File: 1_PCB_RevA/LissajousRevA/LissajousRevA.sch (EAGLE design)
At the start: 0 parts

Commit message: first relax osc and lpf
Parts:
- added C1, C2, C3, C4, C5: (no value), passives:CAP0603-CAP
- added R1, R10, R2, R3, R4, R5, R6, R7, R8, R9: (no value), passives:RESISTOR0603-RES
- added TM1: 200K, adafruit:TRIMPOTTC33X
- added TP1, TP2, TP3: TEST-POINT3, passives:TEST-POINT3
- added U1: LM348D, LM348D:LM348D
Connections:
- new net 0V: C1.1, C2.1, C4.1, R1.1
- new net N$1: C1.2, R3.1, U1D.IN-
- new net N$11: C4.2, R8.1, U1B.IN+
- new net N$12: C5.1, R5.1, R8.2
- new net N$13: C5.2, TP3.1, U1B.IN-, U1B.OUT
- new net N$14: R10.1, R5.2
- new net N$2: R1.2, R2.1, U1D.IN+
- new net N$3: R6.2, R9.1
- new net N$4: R3.2, R4.2, TM1.E, TM1.S
- new net N$5: C2.2, R7.1, U1A.IN+
- new net N$6: C3.1, R6.1, R7.2
- new net N$7: R2.2, R4.1, R9.2, TM1.A, TP1.1, U1D.OUT
- new net N$8: C3.2, R10.2, TP2.1, U1A.IN-, U1A.OUT
- new net V+: U1A.+
- new net V-: U1A.-

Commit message: added second gen
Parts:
- added C10, C6, C7, C8, C9: (no value), passives:CAP0603-CAP
- added R11, R12, R13, R14, R15, R16, R17, R18, R19, R20: (no value), passives:RESISTOR0603-RES
- added TM2: 200K, adafruit:TRIMPOTTC33X
- added TP4, TP5, TP6: TEST-POINT3, passives:TEST-POINT3
- added U2: LM348D, LM348D:LM348D
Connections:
- net N$13 renamed SINEGEN1
- new net N$10: C6.2, R13.1, U2D.IN-
- new net N$15: R12.2, R14.1, R19.2, TM2.A, TP4.1, U2D.OUT
- new net N$16: C7.2, R16.1, U2A.IN+
- new net N$17: C8.1, R15.1, R16.2
- new net N$18: C9.2, R18.1, U2B.IN+
- new net N$19: C10.1, R17.1, R18.2
- new net N$21: C8.2, R20.2, TP5.1, U2A.IN-, U2A.OUT
- new net N$22: R15.2, R19.1
- new net N$23: R17.2, R20.1
- new net N$24: R13.2, R14.2, TM2.E, TM2.S
- new net N$9: R11.2, R12.1, U2D.IN+
- new net SINEGEN2: C10.2, TP6.1, U2B.IN-, U2B.OUT
- net 0V: now also C6.1, C7.1, C9.1, R11.1
- net V+: now also U2A.+
- net V-: now also U2A.-
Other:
- note added: "Sine generation 1"
- note added: "Sine generation 2"
- moved on the sheet: C1, C2, C3, C4, C5, R1, R10, R2, R3, R4, R5, R6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

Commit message: schmatics have everything down
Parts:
- removed C1, C10, C2, C3, C4, C5, C6, C7, C8, C9: (no value), passives:CAP0603-CAP
- removed R1, R10, R11, R12, R13, R14, R15, R16, R17, R18, R19, R2, R20, R3, R4, R5, R6, R7, R8, R9: (no value), passives:RESISTOR0603-RES
- removed TM1, TM2: 200K, adafruit:TRIMPOTTC33X
- removed TP5, TP6: TEST-POINT3, passives:TEST-POINT3
- removed U1, U2: LM348D, LM348D:LM348D
- added C101, C102, C103, C104, C105, C201, C202, C203, C204, C205: 4.7nF, passives:CAP0603-CAP
- added C301, C302, C303, C304, C305, C306, C402: 100nF, passives:CAP0603-CAP
- added C401: 100pF, passives:CAP0603-CAP
- added C501, C502, C503, C504, C505, C506: 10nF, passives:CAP0603-CAP
- added D401: 1N4148, adafruit:DIODESMA
- added Q401, Q501, Q502, Q503: (no value), adafruit:MOSFET-NREFLOW
- added R101, R201, R403, R405, R407: DNF, passives:RESISTOR0603-RES
- added R102, R202, R408, R503: 200K, adafruit:TRIMPOTTC33X
- added R103: 5K, passives:RESISTOR0603-RES
- added R104, R105, R107, R108, R110, R111, R204, R205, R207, R208, R210, R211, R501, R502, R504, R505, R506, R507, R508, R509, R510: 33K, passives:RESISTOR0603-RES
- added R106, R109, R206, R209, R402: 0R, passives:RESISTOR0603-RES
- added R203, R406: 5K6, passives:RESISTOR0603-RES
- added R401: 1M, passives:RESISTOR0603-RES
- added R404: 100K, passives:RESISTOR0603-RES
- added TP101, TP102, TP103, TP201, TP202, TP203, TP401, TP402: TEST-POINT3, passives:TEST-POINT3
- added TP301, TP302, TP303: TEST-POINTTP_15TH_THRU, passives:TEST-POINTTP_15TH_THRU
- added U101, U201, U401: LM348D, LM348D:LM348D
- TP3, TP4: value TEST-POINT3 -> TEST-POINTTP_15TH_THRU; device passives:TEST-POINT3 -> passives:TEST-POINTTP_15TH_THRU
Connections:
- new net N$13: R401.2, R402.1, U101C.IN-
- new net N$20: C501.1, Q501.D, U401A.IN+
- new net N$25: C402.2, R406.2, R407.2, U401C.IN-
- new net N$26: R501.2, R502.1, U401A.IN-
- new net N$27: R404.2, U401B.IN-
- new net N$28: D401.A, U401B.OUT
- new net N$29: C502.1, C503.2, R504.2, R505.1, TP1.1
- new net N$30: C401.2, D401.C, R404.1, R405.1, R406.1, TP401.1
- new net N$31: Q401.D, R402.2, R403.1
- new net N$32: C402.1, Q401.G, R407.1, TP402.1, U401C.OUT
- new net N$33: C502.2, R502.2, U401A.OUT
- new net N$34: R408.S, U401C.IN+
- new net N$35: C506.2
- new net N$36: C503.1, Q502.D, U401D.IN+
- new net N$37: R505.2, R506.1, U401D.IN-
- new net N$38: Q501.G, Q502.G, Q503.G, R503.S
- new net N$39: R506.2, U401D.OUT
- new net N$40: R508.2, R509.1, U201C.IN-
- new net N$41: C504.2
- new net N$42: C504.1, C505.2, R507.2, R508.1, TP2.1
- new net N$45: C505.1, Q503.D, U201C.IN+
- new net N$46: R509.2, U201C.OUT
- new net VIEW1: R401.1, TP4.1, U101C.OUT, U401B.IN+
- new net VIEW2: C506.1, R510.2, TP3.1
- net 0V: now also C101.1, C103.1, C105.1, C201.1, C203.1, C205.1, C301.1, C302.1, C303.1, C304.2, C305.2, C306.2, C401.1, Q401.S, Q501.S, Q502.S, Q503.S, R105.1, R205.1, R403.2, R405.2, R408.E, R503.A, R504.1, R507.1, R510.1, TP302.1; no longer C1.1, C2.1, C4.1, C6.1, C7.1, C9.1, R1.1, R11.1
- net N$1: now also C101.2, R103.1, U101D.IN-; no longer C1.2, R3.1, U1D.IN-
- net N$10: now also C201.2, R203.1, U201D.IN-; no longer C6.2, R13.1, U2D.IN-
- net N$11: now also C105.2, R111.1, U101B.IN+; no longer C4.2, R8.1, U1B.IN+
- net N$12: now also C104.1, R110.1, R111.2; no longer C5.1, R5.1, R8.2
- net N$14: now also R109.1, R110.2; no longer R10.1, R5.2
- net N$15: now also R201.1, R202.A, R204.2, R206.2, TP201.1, U201D.OUT; no longer R12.2, R14.1, R19.2, TM2.A, TP4.1, U2D.OUT
- net N$16: now also C203.2, R208.1, U201A.IN+; no longer C7.2, R16.1, U2A.IN+
- net N$17: now also C202.1, R207.1, R208.2; no longer C8.1, R15.1, R16.2
- net N$18: now also C205.2, R211.1, U201B.IN+; no longer C9.2, R18.1, U2B.IN+
- net N$19: now also C204.1, R210.1, R211.2; no longer C10.1, R17.1, R18.2
- net N$2: now also R104.1, R105.2, U101D.IN+; no longer R1.2, R2.1, U1D.IN+
- net N$21: now also C202.2, R209.2, TP202.1, U201A.IN-, U201A.OUT; no longer C8.2, R20.2, TP5.1, U2A.IN-, U2A.OUT
- net N$22: now also R206.1, R207.2; no longer R15.2, R19.1
- net N$23: now also R209.1, R210.2; no longer R17.2, R20.1
- net N$24: now also R201.2, R202.E, R202.S, R203.2; no longer R13.2, R14.2, TM2.E, TM2.S
- net N$3: now also R106.1, R107.2; no longer R6.2, R9.1
- net N$4: now also R101.2, R102.E, R102.S, R103.2; no longer R3.2, R4.2, TM1.E, TM1.S
- net N$5: now also C103.2, R108.1, U101A.IN+; no longer C2.2, R7.1, U1A.IN+
- net N$6: now also C102.1, R107.1, R108.2; no longer C3.1, R6.1, R7.2
- net N$7: now also R101.1, R102.A, R104.2, R106.2, TP101.1, U101D.OUT; no longer R2.2, R4.1, R9.2, TM1.A, TP1.1, U1D.OUT
- net N$8: now also C102.2, R109.2, TP102.1, U101A.IN-, U101A.OUT; no longer C3.2, R10.2, TP2.1, U1A.IN-, U1A.OUT
- net N$9: now also R204.1, R205.2, U201D.IN+; no longer R11.2, R12.1, U2D.IN+
- net SINEGEN1: now also C104.2, TP103.1, U101B.IN-, U101B.OUT, U101C.IN+; no longer C5.2, TP3.1, U1B.IN-, U1B.OUT
- net SINEGEN2: now also C204.2, C501.2, R501.1, TP203.1, U201B.IN-, U201B.OUT; no longer C10.2, TP6.1, U2B.IN-, U2B.OUT
- net V+: now also C301.2, C302.2, C303.2, R408.A, R503.E, TP301.1, U101A.+, U201A.+, U401A.+; no longer U1A.+, U2A.+
- net V-: now also C304.1, C305.1, C306.1, TP303.1, U101A.-, U201A.-, U401A.-; no longer U1A.-, U2A.-
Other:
- note added: "Automatic gain control"
- note added: "Phase shift"
- note added: "Support"
- moved on the sheet: TP1, TP2, TP3, TP4

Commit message: schematic capture done
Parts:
- renumbered TP1 to TP501, TP2 to TP502, TP3 to TP305, TP4 to TP304
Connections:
- net 0V: now also TP303.1; no longer TP302.1
- net V-: now also TP302.1; no longer TP303.1
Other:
- moved on the sheet: TP302, TP303
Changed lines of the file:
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@@
 <part name="TP203" library="passives" deviceset="TEST-POINT" device="3"/>
 <part name="TP301" library="passives" deviceset="TEST-POINT" device="TP_15TH_THRU"/>
-<part name="TP302" library="passives" deviceset="TEST-POINT" device="TP_15TH_THRU"/>
+<part name="TP303" library="passives" deviceset="TEST-POINT" device="TP_15TH_THRU"/>
 <part name="C301" library="passives" deviceset="CAP" device="0603-CAP" value="100nF"/>
 <part name="C302" library="passives" deviceset="CAP" device="0603-CAP" value="100nF"/>
@@
 <part name="V12" library="supply" deviceset="V+" device=""/>
 <part name="V13" library="supply" deviceset="V-" device=""/>
-<part name="TP303" library="passives" deviceset="TEST-POINT" device="TP_15TH_THRU"/>
+<part name="TP302" library="passives" deviceset="TEST-POINT" device="TP_15TH_THRU"/>
 <part name="C303" library="passives" deviceset="CAP" device="0603-CAP" value="100nF"/>
 <part name="C304" library="passives" deviceset="CAP" device="0603-CAP" value="100nF"/>
@@
 <part name="R510" library="passives" deviceset="RESISTOR" device="0603-RES" value="33K"/>
 <part name="V31" library="supply" deviceset="0V" device=""/>
-<part name="TP1" library="passives" deviceset="TEST-POINT" device="3"/>
-<part name="TP2" library="passives" deviceset="TEST-POINT" device="3"/>
-<part name="TP3" library="passives" deviceset="TEST-POINT" device="TP_15TH_THRU"/>
-<part name="TP4" library="passives" deviceset="TEST-POINT" device="TP_15TH_THRU"/>
+<part name="TP501" library="passives" deviceset="TEST-POINT" device="3"/>
+<part name="TP502" library="passives" deviceset="TEST-POINT" device="3"/>
+<part name="TP305" library="passives" deviceset="TEST-POINT" device="TP_15TH_THRU"/>
+<part name="TP304" library="passives" deviceset="TEST-POINT" device="TP_15TH_THRU"/>
 </parts>
 <sheets>
@@
 <instance part="TP203" gate="G$1" x="256.54" y="152.4"/>
 <instance part="TP301" gate="G$1" x="317.5" y="243.84"/>
-<instance part="TP302" gate="G$1" x="340.36" y="226.06"/>
+<instance part="TP303" gate="G$1" x="340.36" y="226.06"/>
 <instance part="C301" gate="G$1" x="302.26" y="205.74" rot="R180"/>
 <instance part="C302" gate="G$1" x="314.96" y="205.74" rot="R180"/>
@@
 <instance part="V12" gate="1" x="297.18" y="243.84" rot="R90"/>
 <instance part="V13" gate="1" x="297.18" y="236.22" rot="R270"/>
-<instance part="TP303" gate="G$1" x="317.5" y="236.22"/>
+<instance part="TP302" gate="G$1" x="317.5" y="236.22"/>
 <instance part="C303" gate="G$1" x="327.66" y="205.74" rot="R180"/>
 <instance part="C304" gate="G$1" x="340.36" y="205.74" rot="R180"/>
@@
 <instance part="R510" gate="G$1" x="350.52" y="109.22" rot="R90"/>
 <instance part="V31" gate="1" x="350.52" y="99.06"/>
-<instance part="TP1" gate="G$1" x="266.7" y="78.74" rot="R180"/>
-<instance part="TP2" gate="G$1" x="347.98" y="86.36"/>
-<instance part="TP3" gate="G$1" x="325.12" y="175.26" rot="R180"/>
-<instance part="TP4" gate="G$1" x="332.74" y="182.88"/>
+<instance part="TP501" gate="G$1" x="266.7" y="78.74" rot="R180"/>
+<instance part="TP502" gate="G$1" x="347.98" y="86.36"/>
+<instance part="TP305" gate="G$1" x="325.12" y="175.26" rot="R180"/>
+<instance part="TP304" gate="G$1" x="332.74" y="182.88"/>
 </instances>
 <busses>
@@
 </segment>
 <segment>
-<pinref part="TP303" gate="G$1" pin="1"/>
+<pinref part="TP302" gate="G$1" pin="1"/>
 <wire x1="317.5" y1="236.22" x2="299.72" y2="236.22" width="0.1524" layer="91"/>
 <pinref part="V13" gate="1" pin="V-"/>
@@
 </segment>
 <segment>
-<pinref part="TP302" gate="G$1" pin="1"/>
+<pinref part="TP303" gate="G$1" pin="1"/>
 <wire x1="340.36" y1="226.06" x2="322.58" y2="226.06" width="0.1524" layer="91"/>
 <pinref part="V11" gate="1" pin="0V"/>
@@
 </segment>
 <segment>
-<pinref part="TP4" gate="G$1" pin="1"/>
+<pinref part="TP304" gate="G$1" pin="1"/>
 <wire x1="332.74" y1="182.88" x2="314.96" y2="182.88" width="0.1524" layer="91"/>
 <label x="317.5" y="182.88" size="1.778" layer="95"/>
@@
 <junction x="264.16" y="58.42"/>
 <junction x="271.78" y="58.42"/>
-<pinref part="TP1" gate="G$1" pin="1"/>
+<pinref part="TP501" gate="G$1" pin="1"/>
 <wire x1="271.78" y1="78.74" x2="266.7" y2="78.74" width="0.1524" layer="91"/>
 <junction x="271.78" y="78.74"/>
@@
 <wire x1="299.72" y1="124.46" x2="299.72" y2="149.86" width="0.1524" layer="91"/>
 <junction x="299.72" y="124.46"/>
-<pinref part="TP2" gate="G$1" pin="1"/>
+<pinref part="TP502" gate="G$1" pin="1"/>
 <wire x1="347.98" y1="86.36" x2="337.82" y2="86.36" width="0.1524" layer="91"/>
 <junction x="337.82" y="86.36"/>
@@
 </segment>
 <segment>
-<pinref part="TP3" gate="G$1" pin="1"/>
+<pinref part="TP305" gate="G$1" pin="1"/>
 <wire x1="325.12" y1="175.26" x2="347.98" y2="175.26" width="0.1524" layer="91"/>
 <label x="337.82" y="175.26" size="1.778" layer="95"/>

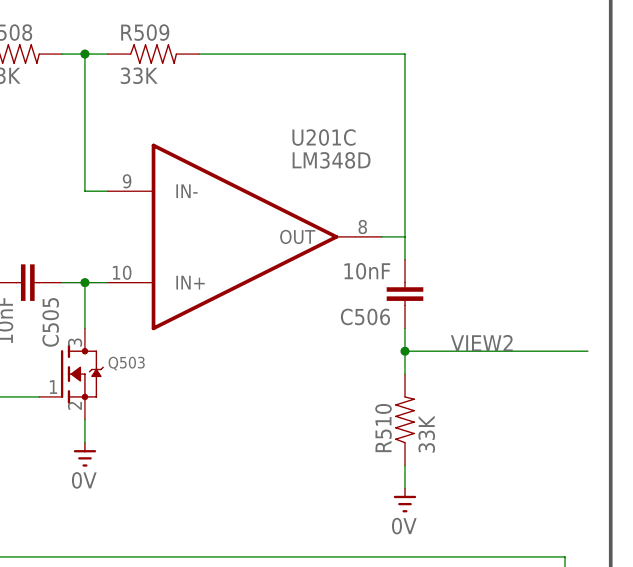
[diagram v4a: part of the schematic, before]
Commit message: sch net fix and more placement
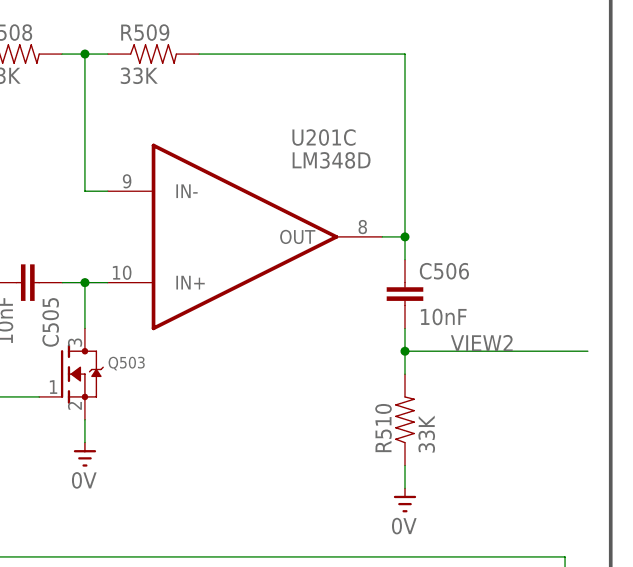
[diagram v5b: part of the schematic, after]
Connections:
- removed net N$35: C506.2
- net N$46: now also C506.1
- net VIEW2: now also C506.2; no longer C506.1
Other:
- moved on the sheet: C506
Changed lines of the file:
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@@
 <part name="R508" library="passives" deviceset="RESISTOR" device="0603-RES" value="33K"/>
 <part name="R509" library="passives" deviceset="RESISTOR" device="0603-RES" value="33K"/>
-<part name="C506" library="passives" deviceset="CAP" device="0603-CAP" value="10nF"/>
 <part name="R510" library="passives" deviceset="RESISTOR" device="0603-RES" value="33K"/>
 <part name="V31" library="supply" deviceset="0V" device=""/>
@@
 <part name="TP305" library="passives" deviceset="TEST-POINT" device="TP_15TH_THRU"/>
 <part name="TP304" library="passives" deviceset="TEST-POINT" device="TP_15TH_THRU"/>
+<part name="C506" library="passives" deviceset="CAP" device="0603-CAP" value="10nF"/>
 </parts>
 <sheets>
@@
 <instance part="R508" gate="G$1" x="307.34" y="149.86"/>
 <instance part="R509" gate="G$1" x="322.58" y="149.86"/>
-<instance part="C506" gate="G$1" x="350.52" y="124.46" rot="R180"/>
 <instance part="R510" gate="G$1" x="350.52" y="109.22" rot="R90"/>
 <instance part="V31" gate="1" x="350.52" y="99.06"/>
@@
 <instance part="TP305" gate="G$1" x="325.12" y="175.26" rot="R180"/>
 <instance part="TP304" gate="G$1" x="332.74" y="182.88"/>
+<instance part="C506" gate="G$1" x="350.52" y="121.92"/>
 </instances>
 <busses>
@@
 <pinref part="R509" gate="G$1" pin="2"/>
 <wire x1="350.52" y1="149.86" x2="327.66" y2="149.86" width="0.1524" layer="91"/>
+<pinref part="C506" gate="G$1" pin="1"/>
+<wire x1="350.52" y1="127" x2="350.52" y2="129.54" width="0.1524" layer="91"/>
 <pinref part="U201" gate="C" pin="OUT"/>
+<wire x1="350.52" y1="129.54" x2="350.52" y2="149.86" width="0.1524" layer="91"/>
 <wire x1="347.98" y1="129.54" x2="350.52" y2="129.54" width="0.1524" layer="91"/>
-<wire x1="350.52" y1="129.54" x2="350.52" y2="149.86" width="0.1524" layer="91"/>
-</segment>
-</net>
-<net name="N$35" class="0">
-<segment>
-<wire x1="350.52" y1="129.54" x2="350.52" y2="127" width="0.1524" layer="91"/>
-<pinref part="C506" gate="G$1" pin="2"/>
+<junction x="350.52" y="129.54"/>
 </segment>
 </net>
@@
 <pinref part="R510" gate="G$1" pin="2"/>
 <wire x1="350.52" y1="114.3" x2="350.52" y2="116.84" width="0.1524" layer="91"/>
-<pinref part="C506" gate="G$1" pin="1"/>
 <wire x1="350.52" y1="116.84" x2="350.52" y2="119.38" width="0.1524" layer="91"/>
 <wire x1="350.52" y1="116.84" x2="370.84" y2="116.84" width="0.1524" layer="91"/>
 <junction x="350.52" y="116.84"/>
 <label x="355.6" y="116.84" size="1.778" layer="95"/>
-</segment>
-<segment>
+<pinref part="C506" gate="G$1" pin="2"/>
+</segment>
+<segment>

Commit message: lots of routing and another net fix
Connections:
- removed net N$41: C504.2
- net N$39: now also C504.2
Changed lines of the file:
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@@
 <net name="N$39" class="0">
 <segment>
-<pinref part="U401" gate="D" pin="OUT"/>
-<wire x1="320.04" y1="58.42" x2="322.58" y2="58.42" width="0.1524" layer="91"/>
-<wire x1="322.58" y1="58.42" x2="322.58" y2="78.74" width="0.1524" layer="91"/>
 <pinref part="R506" gate="G$1" pin="2"/>
 <wire x1="322.58" y1="78.74" x2="299.72" y2="78.74" width="0.1524" layer="91"/>
+<pinref part="U401" gate="D" pin="OUT"/>
+<pinref part="C504" gate="G$1" pin="2"/>
+<wire x1="320.04" y1="58.42" x2="322.58" y2="58.42" width="0.1524" layer="91"/>
+<wire x1="322.58" y1="58.42" x2="325.12" y2="58.42" width="0.1524" layer="91"/>
+<wire x1="322.58" y1="78.74" x2="322.58" y2="58.42" width="0.1524" layer="91"/>
+<junction x="322.58" y="58.42"/>
 </segment>
 </net>
-<net name="N$41" class="0">
-<segment>
-<pinref part="C504" gate="G$1" pin="2"/>
-<wire x1="325.12" y1="58.42" x2="322.58" y2="58.42" width="0.1524" layer="91"/>
-</segment>
-</net>
